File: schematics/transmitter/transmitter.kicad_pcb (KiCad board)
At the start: 4 copper layers, 38 x 80 mm, 27 parts, among them Q1 2N7000, SW1 SW_Nidec_CAS-120A1, SW2 SW_Push, U1 PIC16F18324-xSL, U2 NRF24L01_Breakout, U3 LM2937xT

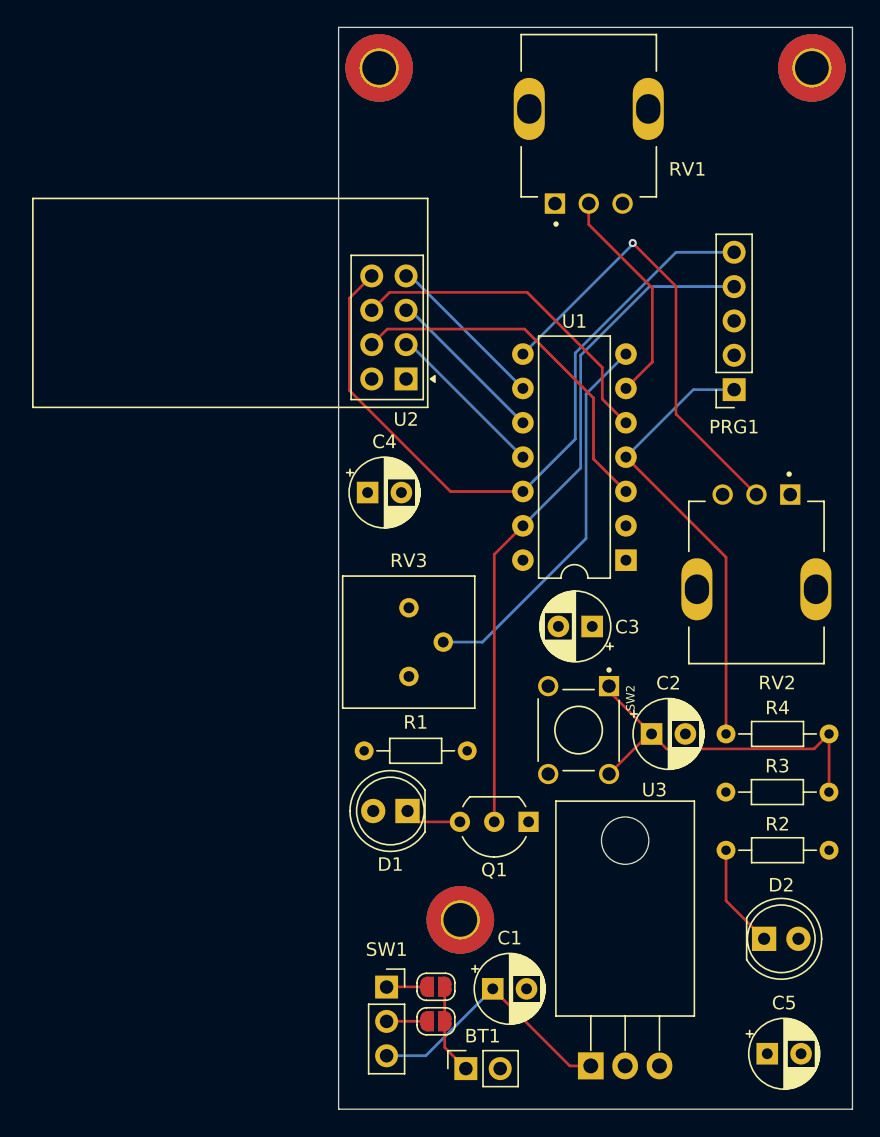
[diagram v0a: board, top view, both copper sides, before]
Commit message: Remove unnecessary devices
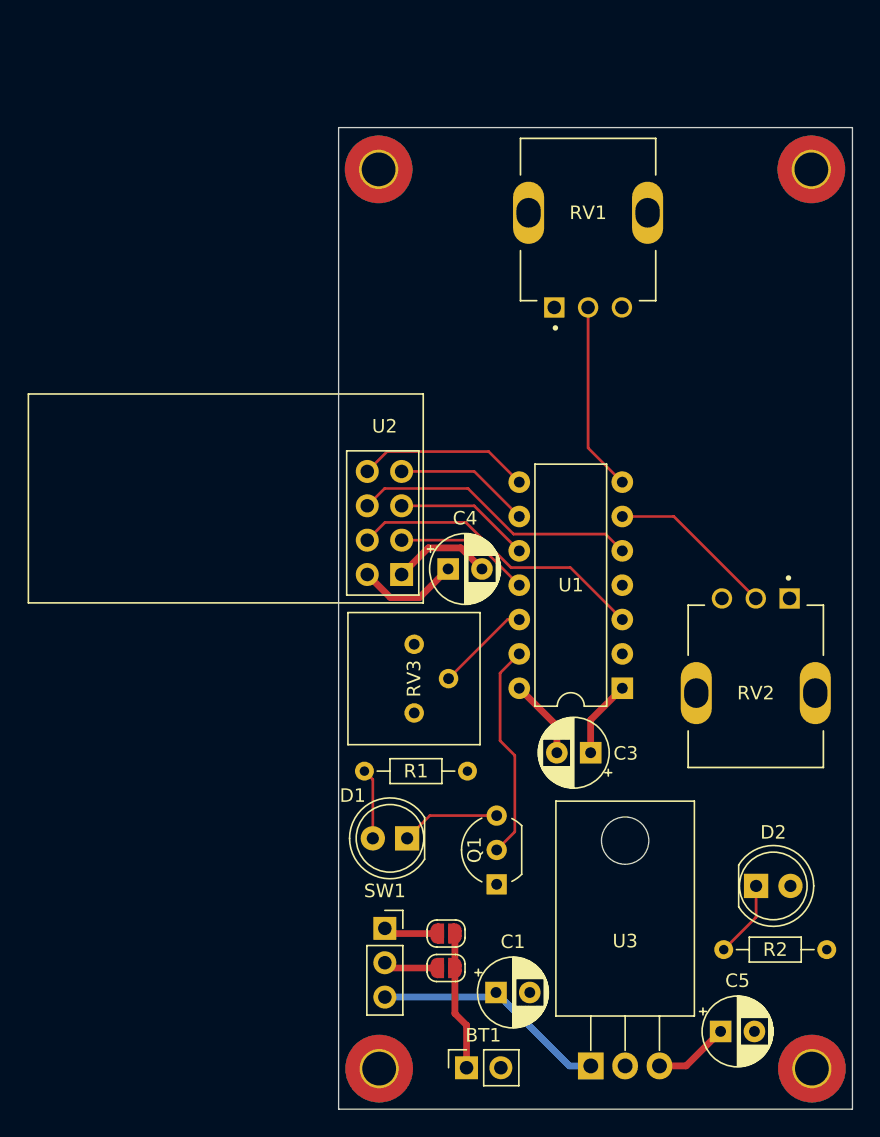
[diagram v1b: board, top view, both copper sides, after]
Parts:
- removed C2: 0.1u, Capacitor_THT:CP_Radial_D5.0mm_P2.50mm
- removed PRG1: MPLAB_Snap, Connector_PinSocket_2.54mm:PinSocket_1x05_P2.54mm_Vertical
- removed R3: 10k, Resistor_THT:R_Axial_DIN0204_L3.6mm_D1.6mm_P7.62mm_Horizontal
- removed R4: 1k, Resistor_THT:R_Axial_DIN0204_L3.6mm_D1.6mm_P7.62mm_Horizontal
- removed SW2: SW_Push, transmitter_footprints:SW_1825910-6-4
- added H4: MountingHole_Pad, MountingHole:MountingHole_2.5mm_Pad_TopBottom, F.Cu at (108.0, 120.0)
- moved U2 14.5 mm to (77.7, 83.5)
- moved H3 12.5 mm to (76.0, 120.0)
- moved U1 9.47 mm to (94.0, 91.9)
- moved C3 9.34 mm to (91.6, 96.6)
- moved C4 8.21 mm to (81.1, 83.0)
- moved RV2 7.68 mm to (103.8, 92.2)
- moved RV1 7.68 mm to (91.5, 56.7)
- moved H1 7.50 mm to (76.0, 53.5)
- moved H2 7.50 mm to (108.0, 53.5)
- moved R2 7.35 mm to (101.5, 111.2)
- moved Q1 5.19 mm to (84.7, 106.4), turned to 90 degrees
- moved SW1 4.34 mm to (76.4, 109.6)
- moved JP1 4.01 mm to (81.0, 112.6)
- moved JP2 4.01 mm to (81.0, 110.0)
- moved D2 3.95 mm to (103.9, 106.5)
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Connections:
- U1 pad 12: IRQ -> STEER_TRIM
- U1 pad 6: STEER -> SPEED
- U1 pad 7: STEER_TRIM -> STEER
- U1 pad 8: SPEED -> IRQ
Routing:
- net IRQ: track 51.8 -> 12.8 mm
- net LED: track 50.6 -> 16.1 mm
- net ~{MCLR}: track 33.6 -> 0.00 mm
- net Net-(C2-Pad1): track 27.6 -> 0.00 mm
- net SPEED: track 34.0 -> 12.4 mm, vias 1 -> 0
- net STEER_TRIM: track 28.6 -> 7.04 mm
- net +3.3V: track 0.00 -> 18.9 mm
- net GND: track 0.00 -> 13.3 mm
- net Net-(D1-A): track 0.00 -> 5.23 mm
- net CSN: track 26.9 -> 22.4 mm
- net Net-(BT1-+): track 6.70 -> 10.3 mm
- net MOSI: track 24.7 -> 21.3 mm
- net Net-(D1-K): track 4.20 -> 7.32 mm
- net STEER: track 16.4 -> 14.0 mm
- net Net-(D2-K): track 7.72 -> 5.70 mm
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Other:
- board size 38 x 80 mm -> 38 x 72.6 mm

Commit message: Add pull up for TX mcu select
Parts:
- added R5: 10k, Resistor_THT:R_Axial_DIN0204_L3.6mm_D1.6mm_P7.62mm_Horizontal, F.Cu at (101.3, 100.2)
- moved R2 7.48 mm to (101.3, 103.7)
- moved D2 3.23 mm to (103.9, 109.7)
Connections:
- U1 pad 2: +3.3V -> Net-(U1-RA5)
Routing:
- net Net-(U1-RA5): track 0.00 -> 13.9 mm
- net Net-(D2-K): track 5.70 -> 7.08 mm

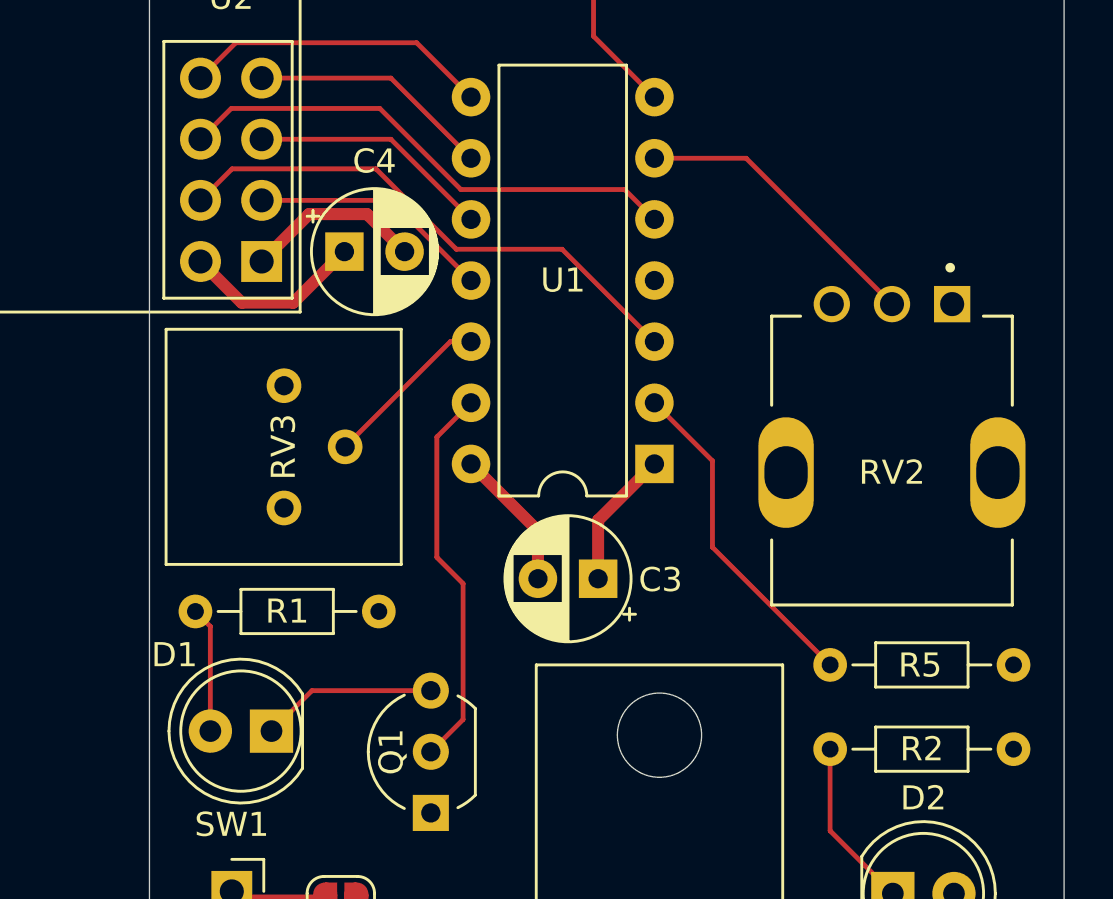
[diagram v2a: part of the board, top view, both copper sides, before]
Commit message: Add pull down for lights on transmitter board
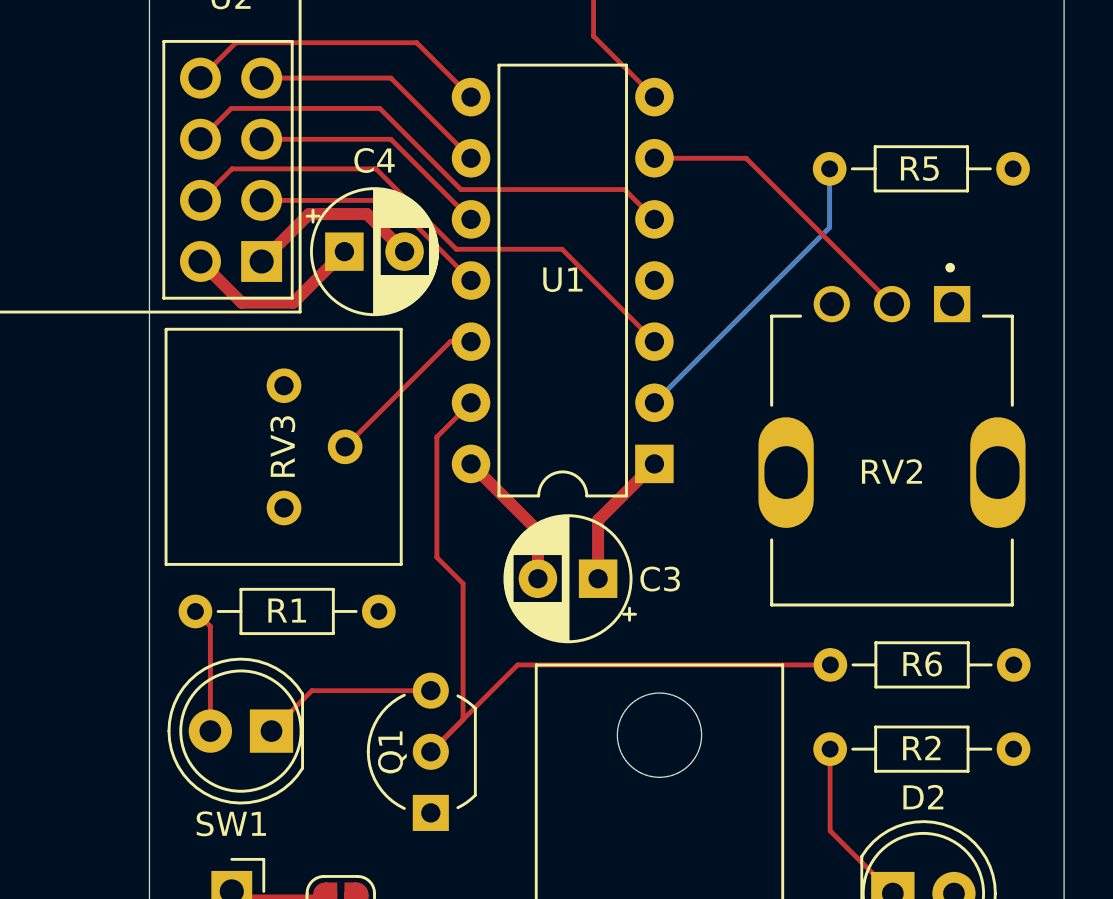
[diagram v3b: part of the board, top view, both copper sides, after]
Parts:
- added R6: 10k, Resistor_THT:R_Axial_DIN0204_L3.6mm_D1.6mm_P7.62mm_Horizontal, F.Cu at (101.3, 100.2)
- moved R5 20.6 mm to (101.3, 79.6)
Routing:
- net LED: track 16.1 -> 34.2 mm
- net Net-(U1-RA5): track 13.9 -> 12.7 mm

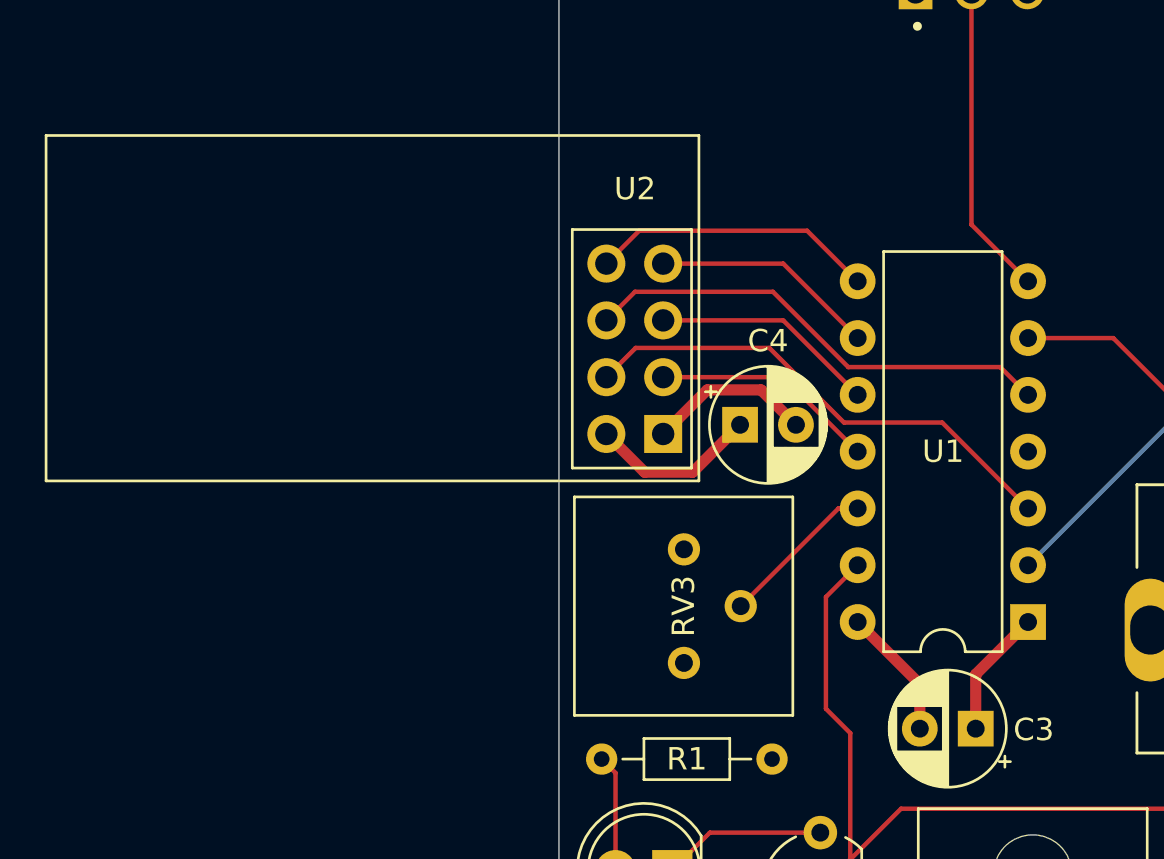
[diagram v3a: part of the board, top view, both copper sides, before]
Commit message: Remove trim pot, seems unnecessary
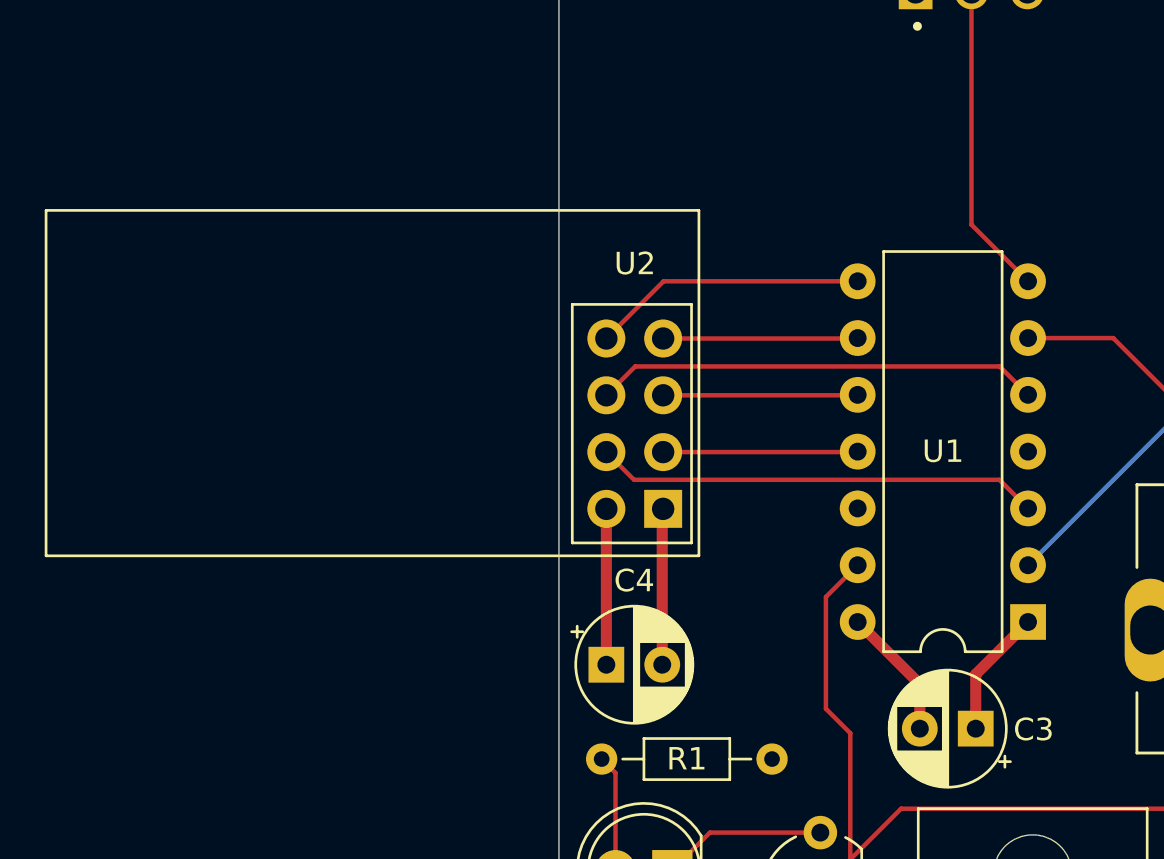
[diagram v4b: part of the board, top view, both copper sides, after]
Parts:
- removed RV3: R_Potentiometer, Potentiometer_THT:Potentiometer_Bourns_3386P_Vertical
- moved C4 12.3 mm to (75.1, 93.8)
- moved U2 3.35 mm to (77.7, 86.8)
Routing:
- net STEER_TRIM: track 7.04 -> 0.00 mm
- net CSN: track 22.4 -> 19.9 mm
- net MOSI: track 21.3 -> 19.9 mm
- net MISO: track 10.1 -> 8.71 mm
- net CE: track 10.1 -> 8.71 mm
- net SCK: track 10.1 -> 8.71 mm
- net +3.3V: track 18.9 -> 18.3 mm

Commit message: Remove programing ports and reset btn from final boards
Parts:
- moved H1 18.3 mm to (75.9, 71.8)
- moved U2 1.91 mm to (77.6, 88.7)
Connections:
- C3 pad 1: +3.3V -> unconnected-(C3-Pad1)
- U1 pad 12: STEER_TRIM -> unconnected-(U1-RA1-Pad12)
- U1 pad 4: ~{MCLR} -> unconnected-(U1-RA3/~{MCLR}-Pad4)
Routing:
- net GND: track 12.9 -> 5.92 mm
- net +3.3V: track 18.3 -> 11.3 mm
- net CE: track 8.71 -> 9.60 mm
- net MOSI: track 19.9 -> 20.8 mm
- net IRQ: track 12.3 -> 13.1 mm
- net SCK: track 8.71 -> 9.54 mm
- net MISO: track 8.71 -> 9.54 mm
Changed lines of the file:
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@@
 	(net 7 "Net-(JP2-B)")
 	(net 8 "LED")
-	(net 9 "STEER_TRIM")
-	(net 10 "~{MCLR}")
+	(net 9 "unconnected-(C3-Pad1)")
+	(net 10 "unconnected-(U1-RA1-Pad12)")
 	(net 11 "Net-(D1-K)")
 	(net 12 "Net-(D1-A)")
@@
 	(net 20 "MOSI")
 	(net 21 "Net-(U1-RA5)")
+	(net 22 "unconnected-(U1-RA3{slash}~{MCLR}-Pad4)")
 	(footprint "Package_TO_SOT_THT:TO-92_Inline_Wide"
 		(layer "F.Cu")
@@
 	(footprint "MountingHole:MountingHole_2.5mm_Pad_TopBottom"
 		(layer "F.Cu")
-		(at 75.96 53.5)
+		(at 75.91 71.78)
 		(descr "Mounting Hole 2.5mm")
 		(tags "mounting hole 2.5mm")
@@
 			(layers "*.Cu" "*.Mask")
 			(remove_unused_layers no)
-			(net 4 "+3.3V")
+			(net 9 "unconnected-(C3-Pad1)")
 			(pintype "passive")
 		)
@@
 			(layers "*.Cu" "*.Mask")
 			(remove_unused_layers no)
-			(net 10 "~{MCLR}")
+			(net 22 "unconnected-(U1-RA3{slash}~{MCLR}-Pad4)")
 			(pinfunction "RA3/~{MCLR}")
-			(pintype "bidirectional")
+			(pintype "bidirectional+no_connect")
 		)
 		(pad "5" thru_hole oval
@@
 			(layers "*.Cu" "*.Mask")
 			(remove_unused_layers no)
-			(net 9 "STEER_TRIM")
+			(net 10 "unconnected-(U1-RA1-Pad12)")
 			(pinfunction "RA1")
-			(pintype "bidirectional")
+			(pintype "bidirectional+no_connect")
 		)
 		(pad "13" thru_hole oval
@@
 	(footprint "RF_Module:nRF24L01_Breakout"
 		(layer "F.Cu")
-		(at 77.66 86.81 180)
+		(at 77.62 88.72 180)
 		(descr "nRF24L01 breakout board")
 		(tags "nRF24L01 adapter breakout")
@@
 		(tags "CP Radial series Radial pin pitch 2.50mm  diameter 5mm Electrolytic Capacitor")
 		(property "Reference" "C4"
-			(at 1.25 -3.75 0)
+			(at 5.01 -0.02 0)
 			(layer "F.SilkS")
 			(effects
@@
 		(model "${KICAD8_3DMODEL_DIR}/LED_THT.3dshapes/LED_D5.0mm.wrl"
 			(offset
-				(xyz 0 0 0)
+				(xyz 0 0 -3)
 			)
 			(scale
@@
 	)
 	(segment
-		(start 77.62 93.78)
-		(end 77.62 86.85)
-		(width 0.5)
-		(layer "F.Cu")
-		(net 2)
-	)
-	(segment
-		(start 77.62 86.85)
-		(end 77.66 86.81)
-		(width 0.2)
-		(layer "F.Cu")
-		(net 2)
-	)
-	(segment
 		(start 76.42 114.71)
 		(end 84.3 114.71)
@@
 	)
 	(segment
-		(start 75.12 93.78)
-		(end 75.12 86.81)
-		(width 0.5)
-		(layer "F.Cu")
-		(net 4)
-	)
-	(segment
 		(start 101.28 107.115)
 		(end 103.885 109.72)
@@
 	)
 	(segment
-		(start 86.34 84.27)
+		(start 82.81 84.25)
 		(end 86.36 84.25)
 		(width 0.2)
@@
 	)
 	(segment
-		(start 77.66 84.27)
-		(end 86.34 84.27)
+		(start 77.62 86.18)
+		(end 80.88 86.18)
+		(width 0.2)
+		(layer "F.Cu")
+		(net 15)
+	)
+	(segment
+		(start 80.88 86.18)
+		(end 82.81 84.25)
 		(width 0.2)
 		(layer "F.Cu")
@@
 	)
 	(segment
-		(start 75.12 79.19)
-		(end 77.68 76.63)
+		(start 77.62 86.85)
+		(end 77.66 86.81)
+		(width 0.2)
+		(layer "F.Cu")
+		(net 15)
+	)
+	(segment
+		(start 75.08 81.1)
+		(end 79.55 76.63)
 		(width 0.2)
 		(layer "F.Cu")
@@
 	)
 	(segment
-		(start 77.68 76.63)
+		(start 79.55 76.63)
 		(end 86.36 76.63)
 		(width 0.2)
@@
 	)
 	(segment
-		(start 77.66 81.73)
-		(end 86.34 81.73)
+		(start 81.18 83.64)
+		(end 83.11 81.71)
 		(width 0.2)
 		(layer "F.Cu")
@@
 	)
 	(segment
-		(start 86.34 81.73)
+		(start 83.11 81.71)
 		(end 86.36 81.71)
 		(width 0.2)
@@
 	)
 	(segment
-		(start 86.34 79.19)
-		(end 86.36 79.17)
+		(start 77.62 83.64)
+		(end 81.18 83.64)
+		(width 0.2)
+		(layer "F.Cu")
+		(net 17)
+	)
+	(segment
+		(start 81.57 81.1)
+		(end 83.5 79.17)
+		(width 0.2)
+		(layer "F.Cu")
+		(net 18)
+	)
+	(segment
+		(start 77.62 81.1)
+		(end 81.57 81.1)
 		(width 0.2)
 		(layer "F.Cu")
@@
 	)
 	(segment
-		(start 77.66 79.19)
-		(end 86.34 79.19)
+		(start 83.5 79.17)
+		(end 86.36 79.17)
 		(width 0.2)
 		(layer "F.Cu")
@@
 	)
 	(segment
-		(start 92.7 85.51)
+		(start 76.31 87.41)
+		(end 82.64 87.41)
+		(width 0.2)
+		(layer "F.Cu")
+		(net 19)
+	)
+	(segment
+		(start 75.08 86.18)
+		(end 76.31 87.41)
+		(width 0.2)
+		(layer "F.Cu")
+		(net 19)
+	)
+	(segment
+		(start 90.49 86.79)
 		(end 93.98 86.79)
 		(width 0.2)
@@
 	)
 	(segment
-		(start 75.12 84.27)
-		(end 76.36 85.51)
+		(start 83.26 88.03)
+		(end 89.25 88.03)
 		(width 0.2)
 		(layer "F.Cu")
@@
 	)
 	(segment
-		(start 76.36 85.51)
-		(end 92.7 85.51)
+		(start 82.64 87.41)
+		(end 83.26 88.03)
 		(width 0.2)
 		(layer "F.Cu")
@@
 	)
 	(segment
-		(start 92.71 80.44)
+		(start 89.25 88.03)
+		(end 90.49 86.79)
+		(width 0.2)
+		(layer "F.Cu")
+		(net 19)
+	)
+	(segment
+		(start 92.66 80.39)
 		(end 93.98 81.71)
 		(width 0.2)
@@
 	)
 	(segment
-		(start 75.12 81.73)
-		(end 76.41 80.44)
+		(start 81.41 82.37)
+		(end 83.39 80.39)
+		(width 0.2)
+		(layer "F.Cu")
+		(net 20)
+	)
+	(segment
+		(start 76.35 82.37)
+		(end 81.41 82.37)
+		(width 0.2)
+		(layer "F.Cu")
+		(net 20)
+	)
+	(segment
+		(start 83.39 80.39)
+		(end 92.66 80.39)
 		(width 0.2)
 		(layer "F.Cu")
@@
 	)
 	(segment
-		(start 76.41 80.44)
-		(end 92.71 80.44)
+		(start 75.08 83.64)
+		(end 76.35 82.37)
 		(width 0.2)
 		(layer "F.Cu")
